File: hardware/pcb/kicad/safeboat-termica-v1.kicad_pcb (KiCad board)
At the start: 2 copper layers, 32 x 32 mm, 32 parts, among them J1 USB 5V D- D+ GND, J2 KF350-3.5-2P, Q1 SI2301, SW1 BOOT, SW2 RST, U1 ESP32-C3-MINI-1-N4, U2 AP63203WU-7, U3 MLX90640ESF-BAA

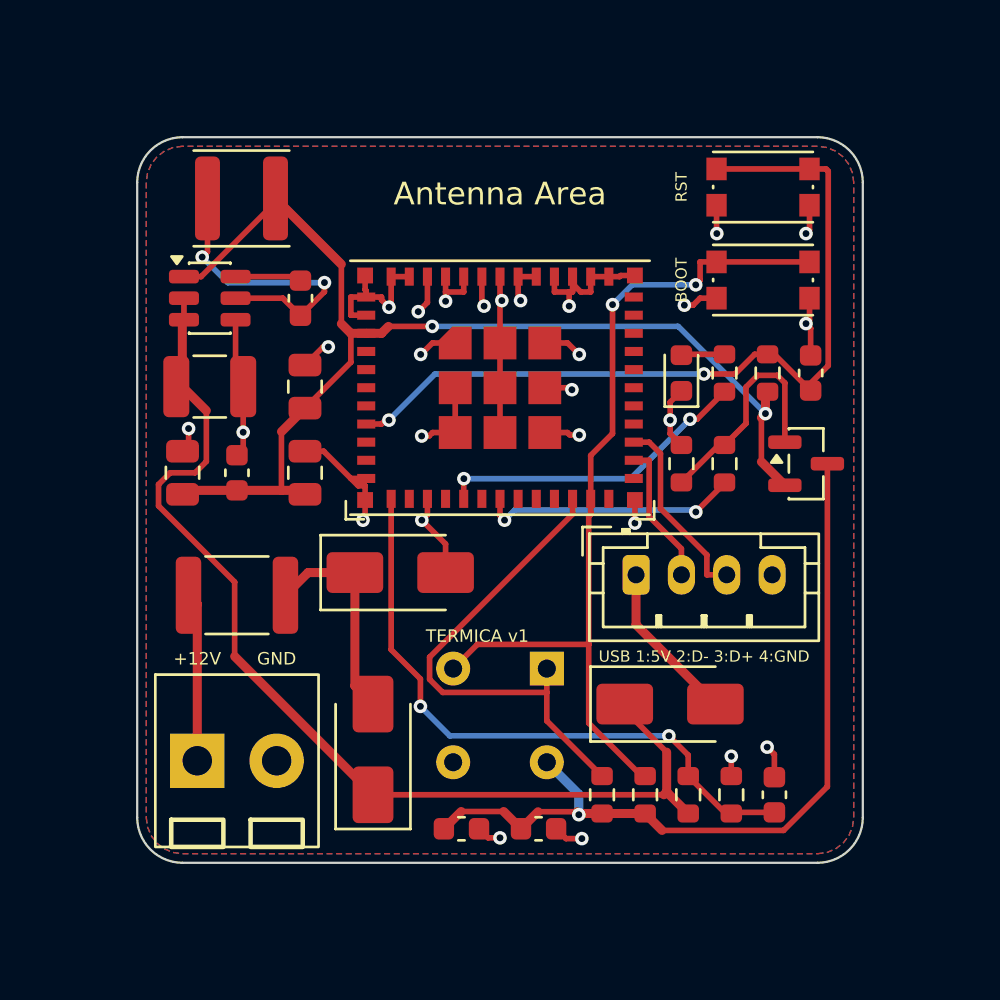
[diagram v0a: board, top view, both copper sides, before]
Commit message: PCB térmica rev. 2: 40×40 mm, 4 camadas, 8–32 V (MP4560), antena com recortes, 4 furos, pads de alimentação
Pedidos da reunião de 22/10: nada metálico ao lado da antena; diretrizes Espressif
(recortes laterais na antena, keep-out em 4 camadas, plano GND sob o módulo);
trilhas a 90° (snap_angle no DSN); planos internos sólidos In1 GND / In2 3V3
(roteador vê só F/B); isolamento 0,2 mm; furos M2,5 longe da antena; PPTC mantido;
MP4560 + SMBJ33A + 4,7 µF/100 V para 8–32 V; borne removido (pads P1/P2).
DRC 0/0/0, ERC 0, netlist esquemático × PCB 0 diferenças. BOM com todos os códigos.
Pacote de revisão regenerado (inclui planos internos).

Co-Authored-By: Claude Fable 5.1 <noreply@anthropic.com>
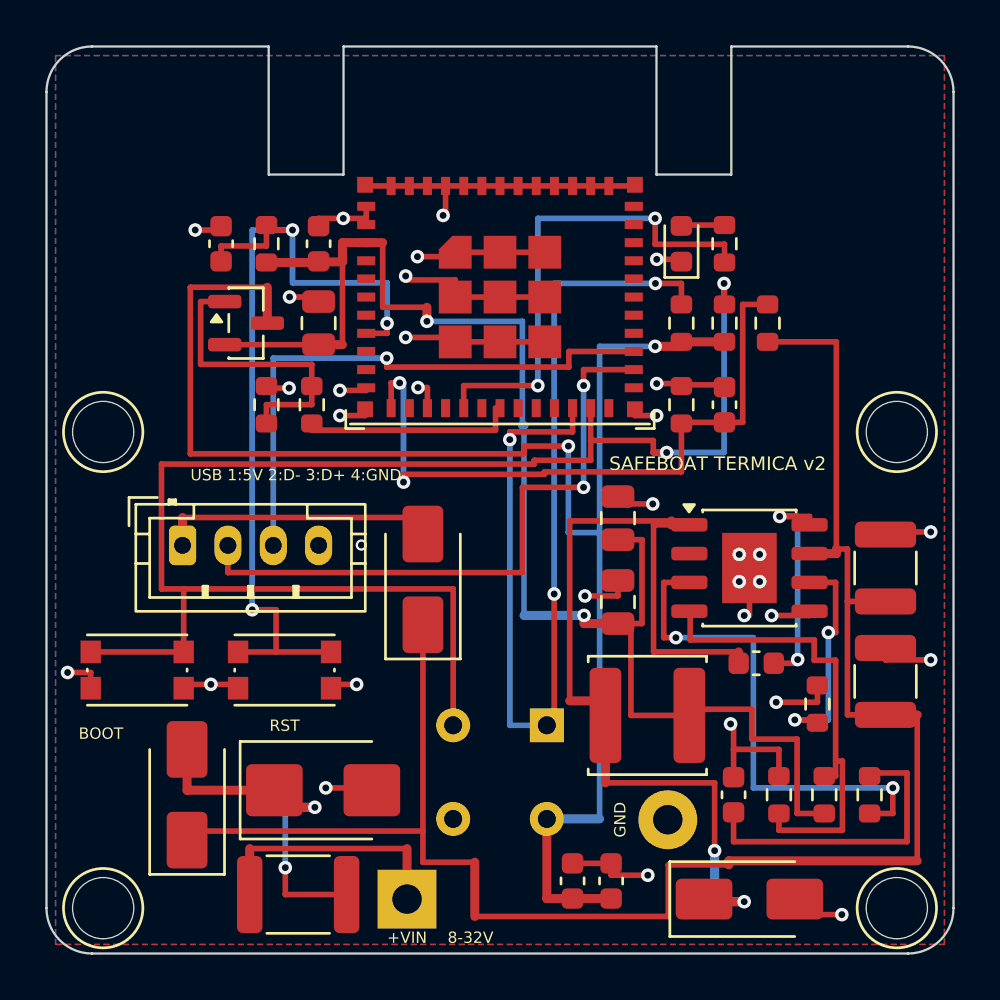
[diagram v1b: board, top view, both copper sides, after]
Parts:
- removed J2: KF350-3.5-2P, SAFEBOAT:KF350-3.5-2P
- added C11: 4.7u/100V, C_1210_3225Metric, F.Cu at (117.0, 108.0)
- added C12: 1n, C_0603_1608Metric, F.Cu at (110.3, 113.0)
- added D4: SS36, D_SMA, F.Cu at (111.0, 117.6)
- added H1: M2.5, SAFEBOAT:MountHole_M2.5_NPTH, F.Cu at (82.5, 97.0)
- added H2: M2.5, SAFEBOAT:MountHole_M2.5_NPTH, F.Cu at (117.5, 97.0)
- added H3: M2.5, SAFEBOAT:MountHole_M2.5_NPTH, F.Cu at (82.5, 118.0)
- added H4: M2.5, SAFEBOAT:MountHole_M2.5_NPTH, F.Cu at (117.5, 118.0)
- added P1: +VIN 8-32V, SAFEBOAT:WirePad_P1, F.Cu at (95.9, 117.6)
- added P2: GND, SAFEBOAT:WirePad_P2, F.Cu at (107.4, 114.1)
- added R10: 15k, R_0603_1608Metric, F.Cu at (112.3, 113.0)
- added R11: 200k, R_0603_1608Metric, F.Cu at (114.0, 109.0)
- added R12: 68k, R_0603_1608Metric, F.Cu at (116.3, 113.0)
- added R9: 47k, R_0603_1608Metric, F.Cu at (114.3, 113.0)
- C5: value 10u/50V -> 4.7u/100V
- D1: value SMAJ26A -> SMBJ33A; footprint D_SMA -> D_SMB
- L1: value 4.7u SWPA4020S -> 10u SWPA5040S; footprint L_Sunlord_SWPA4020S -> L_Sunlord_SWPA5040S
- R7: value 200k -> 330k
- R8: value 20k -> 15k
- U2: value AP63203WU-7 -> MP4560DN; footprint TSOT-23-6 -> HSOP-8-1EP_3.9x4.9mm_P1.27mm_EP2.41x3.1mm
- moved SW1 32.5 mm to (84.0, 107.5)
- moved C5 30.9 mm to (117.0, 103.0), turned to 90 degrees
- moved SW2 30.0 mm to (90.5, 107.5)
- moved L1 29.0 mm to (106.5, 109.5)
- moved C1 26.6 mm to (87.7, 88.7)
- moved U2 26.6 mm to (111.0, 103.0)
- moved C8 25.8 mm to (111.3, 107.2), turned to 0 degrees
- moved Q1 25.5 mm to (88.8, 92.2)
- moved R1 22.8 mm to (89.7, 88.7)
- moved R2 21.1 mm to (108.0, 92.2)
- moved R3 21.1 mm to (109.9, 92.2)
- moved R7 21.1 mm to (111.8, 92.2)
- moved J1 20.0 mm to (86.0, 102.0)
- moved R5 18.5 mm to (89.7, 95.8)
- moved R6 18.4 mm to (91.7, 95.8)
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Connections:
- U2 pad 1: 3V3 -> SW
- U2 pad 2: VIN -> (no net)
- U2 pad 3: VIN -> COMP
- U2 pad 4: GND -> FB
- U2 pad 5: SW -> GND
- U2 pad 6: BST -> FREQ
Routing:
- net VDD_MLX: track 36.2 -> 69.8 mm, vias 1 -> 2
- net VIN: track 47.1 -> 80.5 mm
- net SCL: track 38.7 -> 68.6 mm
- net SW: track 13.6 -> 42.5 mm
- net SDA: track 21.7 -> 44.7 mm, vias 0 -> 3
- net COMP: track 0.00 -> 22.4 mm, vias 0 -> 2
- net USB_DM: track 6.32 -> 28.1 mm, vias 0 -> 2
- net FB: track 0.00 -> 21.1 mm
- net USB_DP: track 8.46 -> 25.2 mm, vias 0 -> 1
- net GND: track 70.5 -> 85.1 mm, vias 27 -> 33
- net 3V3: track 51.3 -> 65.3 mm
- net COMP_C: track 0.00 -> 13.8 mm
- net FREQ: track 0.00 -> 10.1 mm, vias 0 -> 2
- net LED_IO: track 14.0 -> 21.8 mm
- net BST: track 2.93 -> 10.0 mm, vias 0 -> 2
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- added copper zone on In2.Cu, net 3V3
- added copper zone on In1.Cu, net GND
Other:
- board size 32 x 32 mm -> 40 x 40 mm
- copper layers 2 -> 4
- board text added: "+VIN"
- board text added: "8-32V"
- board text added: "SAFEBOAT TERMICA v2"
- board text added: "frente (lata exposta: vedar em volta)"
- board text removed: "+12V"
- board text removed: "SAFEBOAT TERMICA v1"
- board text removed: "TERMICA v1"
- board text removed: "frente: janela de germanio"
